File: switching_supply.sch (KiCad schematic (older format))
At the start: 0 parts

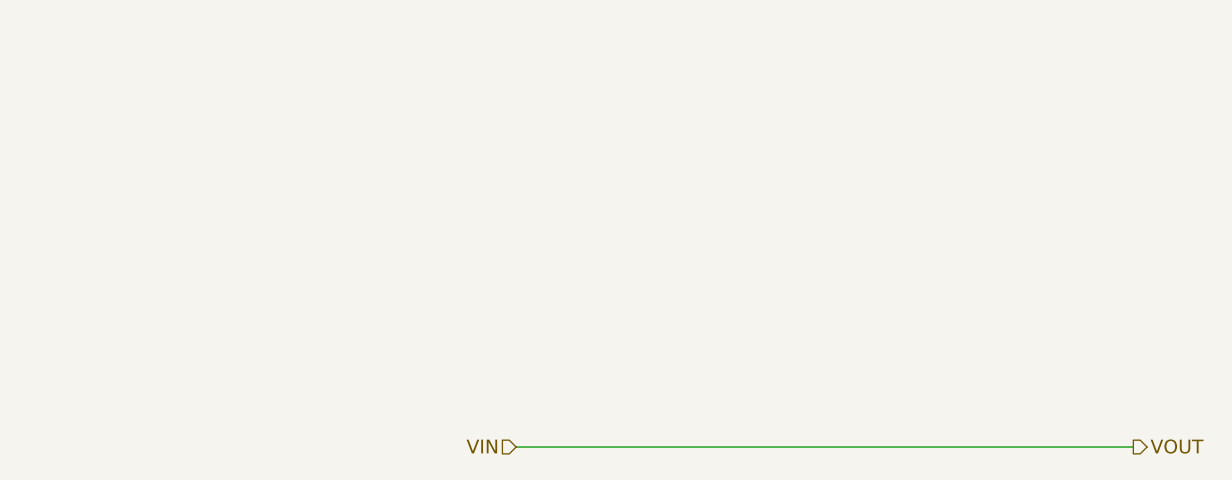
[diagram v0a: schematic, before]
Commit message: Esquematico completo. Footprintss asignados
Signed-off-by: Marcos Chaparro <mchaparro@paltatech.com>
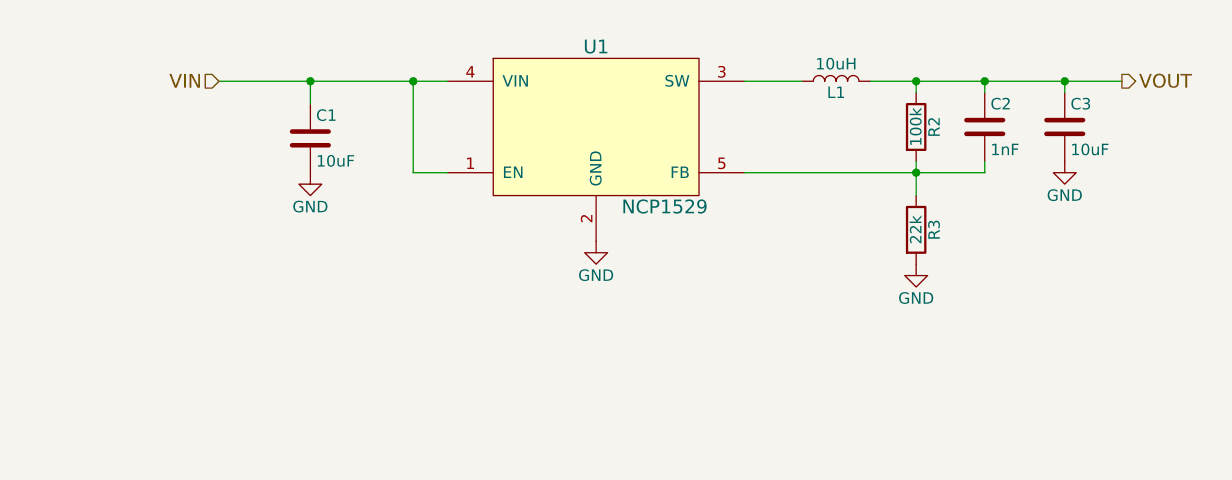
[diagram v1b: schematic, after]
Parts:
- added C1, C3: 10uF, Capacitors_SMD:C_0805, symbol C
- added C2: 1nF, Capacitors_SMD:C_0603, symbol C
- added L1: 10uH, Inductors_SMD:L_1812, symbol L
- added R2: 100k, Resistors_SMD:R_0603, symbol R
- added R3: 22k, Resistors_SMD:R_0603, symbol R
- added U1: NCP1529, TO_SOT_Packages_SMD:SOT-23-5, symbol NCP1529
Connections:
- net VIN: now also C1.1, U1.1 (EN), U1.4 (VIN)
- new net: L1.1, U1.3 (SW)
- new net: C2.2, R2.2, R3.1, U1.5 (FB)
- new net GND: C1.2, C3.2, R3.2, U1.2 (GND)
- new net VOUT: C2.1, C3.1, L1.2, R2.1
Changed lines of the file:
@@
 LIBS:contrib
 LIBS:valves
+LIBS:curso
+LIBS:bichito_e_luz-cache
 EELAYER 25 0
 EELAYER END
@@
 Comment4 ""
 $EndDescr
-Text HLabel 4900 4650 0    60   Input ~ 0
+Text HLabel 3600 3050 0    60   Input ~ 0
 VIN
-Text HLabel 7600 4650 2    60   Output ~ 0
+Text HLabel 7550 3050 2    60   Output ~ 0
 VOUT
+$Comp
+L NCP1529 U1
+U 1 1 59B19714
+P 5250 3350
+F 0 "U1" H 5250 3800 60  0000 C CNN
+F 1 "NCP1529" H 5550 3100 60  0000 C CNN
+F 2 "TO_SOT_Packages_SMD:SOT-23-5" H 5250 3350 60  0001 C CNN
+F 3 "" H 5250 3350 60  0001 C CNN
+	1    5250 3350
+	1    0    0    -1
+$EndComp
+$Comp
+L C C1
+U 1 1 59B1980A
+P 4000 3300
+F 0 "C1" H 4025 3400 50  0000 L CNN
+F 1 "10uF" H 4025 3200 50  0000 L CNN
+F 2 "Capacitors_SMD:C_0805" H 4038 3150 50  0001 C CNN
+F 3 "" H 4000 3300 50  0001 C CNN
+	1    4000 3300
+	1    0    0    -1
+$EndComp
+$Comp
+L L L1
+U 1 1 59B1986B
+P 6300 3050
+F 0 "L1" V 6250 3050 50  0000 C CNN
+F 1 "10uH" V 6375 3050 50  0000 C CNN
+F 2 "Inductors_SMD:L_1812" H 6300 3050 50  0001 C CNN
+F 3 "" H 6300 3050 50  0001 C CNN
+	1    6300 3050
+	0    -1   -1   0
+$EndComp
+$Comp
+L R R2
+U 1 1 59B198DA
+P 6650 3250
+F 0 "R2" V 6730 3250 50  0000 C CNN
+F 1 "100k" V 6650 3250 50  0000 C CNN
+F 2 "Resistors_SMD:R_0603" V 6580 3250 50  0001 C CNN
+F 3 "" H 6650 3250 50  0001 C CNN
+	1    6650 3250
+	1    0    0    -1
+$EndComp
+$Comp
+L R R3
+U 1 1 59B1995B
+P 6650 3700
+F 0 "R3" V 6730 3700 50  0000 C CNN
+F 1 "22k" V 6650 3700 50  0000 C CNN
+F 2 "Resistors_SMD:R_0603" V 6580 3700 50  0001 C CNN
+F 3 "" H 6650 3700 50  0001 C CNN
+	1    6650 3700
+	1    0    0    -1
+$EndComp
+$Comp
+L C C2
+U 1 1 59B1998D
+P 6950 3250
+F 0 "C2" H 6975 3350 50  0000 L CNN
+F 1 "1nF" H 6975 3150 50  0000 L CNN
+F 2 "Capacitors_SMD:C_0603" H 6988 3100 50  0001 C CNN
+F 3 "" H 6950 3250 50  0001 C CNN
+	1    6950 3250
+	1    0    0    -1
+$EndComp
+$Comp
+L C C3
+U 1 1 59B199F3
+P 7300 3250
+F 0 "C3" H 7325 3350 50  0000 L CNN
+F 1 "10uF" H 7325 3150 50  0000 L CNN
+F 2 "Capacitors_SMD:C_0805" H 7338 3100 50  0001 C CNN
+F 3 "" H 7300 3250 50  0001 C CNN
+	1    7300 3250
+	1    0    0    -1
+$EndComp
+$Comp
+L GND #PWR03
+U 1 1 59B19A47
+P 5250 3750
+F 0 "#PWR03" H 5250 3500 50  0001 C CNN
+F 1 "GND" H 5250 3600 50  0000 C CNN
+F 2 "" H 5250 3750 50  0001 C CNN
+F 3 "" H 5250 3750 50  0001 C CNN
+	1    5250 3750
+	1    0    0    -1
+$EndComp
 Wire Wire Line
-	4900 4650 7600 4650
+	3600 3050 4600 3050
+Wire Wire Line
+	4000 3150 4000 3050
+Connection ~ 4000 3050
+$Comp
+L GND #PWR04
+U 1 1 59B19AE4
+P 4000 3450
+F 0 "#PWR04" H 4000 3200 50  0001 C CNN
+F 1 "GND" H 4000 3300 50  0000 C CNN
+F 2 "" H 4000 3450 50  0001 C CNN
+F 3 "" H 4000 3450 50  0001 C CNN
+	1    4000 3450
+	1    0    0    -1
+$EndComp
+Wire Wire Line
+	4600 3450 4450 3450
+Wire Wire Line
+	4450 3450 4450 3050
+Connection ~ 4450 3050
+Wire Wire Line
+	5900 3050 6150 3050
+Wire Wire Line
+	6450 3050 7550 3050
+Wire Wire Line
+	6650 3050 6650 3100
+Wire Wire Line
+	6650 3400 6650 3550
+Wire Wire Line
+	5900 3450 6950 3450
+Connection ~ 6650 3450
+Wire Wire Line
+	6950 3050 6950 3100
+Connection ~ 6650 3050
+Wire Wire Line
+	6950 3450 6950 3400
+Wire Wire Line
+	7300 3050 7300 3100
+Connection ~ 6950 3050
+$Comp
+L GND #PWR05
+U 1 1 59B19BA3
+P 6650 3850
+F 0 "#PWR05" H 6650 3600 50  0001 C CNN
+F 1 "GND" H 6650 3700 50  0000 C CNN
+F 2 "" H 6650 3850 50  0001 C CNN
+F 3 "" H 6650 3850 50  0001 C CNN
+	1    6650 3850
+	1    0    0    -1
+$EndComp
+$Comp
+L GND #PWR06
+U 1 1 59B19BC3
+P 7300 3400
+F 0 "#PWR06" H 7300 3150 50  0001 C CNN
+F 1 "GND" H 7300 3250 50  0000 C CNN
+F 2 "" H 7300 3400 50  0001 C CNN
+F 3 "" H 7300 3400 50  0001 C CNN
+	1    7300 3400
+	1    0    0    -1
+$EndComp
+Connection ~ 7300 3050
 $EndSCHEMATC

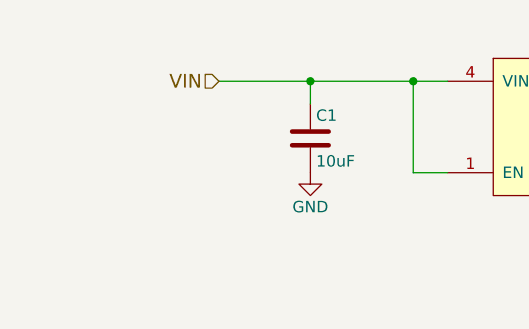
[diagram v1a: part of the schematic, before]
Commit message: Termino layout. Despues de la clase agregue silkscreens y un fusible
Signed-off-by: Marcos Chaparro <mchaparro@paltatech.com>
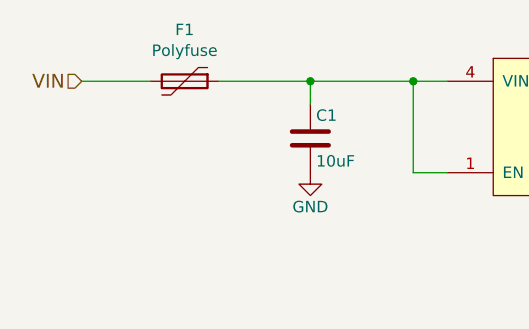
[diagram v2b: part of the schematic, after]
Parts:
- added F1: Polyfuse, Resistors_SMD:R_0805, symbol Polyfuse
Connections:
- net VIN: now also F1.2; no longer C1.1, U1.1 (EN), U1.4 (VIN)
- new net: C1.1, F1.1, U1.1 (EN), U1.4 (VIN)
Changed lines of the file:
@@
 Comment4 ""
 $EndDescr
-Text HLabel 3600 3050 0    60   Input ~ 0
+Text HLabel 3000 3050 0    60   Input ~ 0
 VIN
 Text HLabel 7550 3050 2    60   Output ~ 0
@@
 $EndComp
 Connection ~ 7300 3050
+$Comp
+L Polyfuse F1
+U 1 1 59BA7D61
+P 3450 3050
+F 0 "F1" V 3225 3050 50  0000 C CNN
+F 1 "Polyfuse" V 3316 3050 50  0000 C CNN
+F 2 "Resistors_SMD:R_0805" H 3500 2850 50  0001 L CNN
+F 3 "" H 3450 3050 50  0001 C CNN
+F 4 "0" H 3450 3050 60  0001 C CNN "Exclude from BOM"
+	1    3450 3050
+	0    1    1    0
+$EndComp
+Wire Wire Line
+	3300 3050 3000 3050
 $EndSCHEMATC

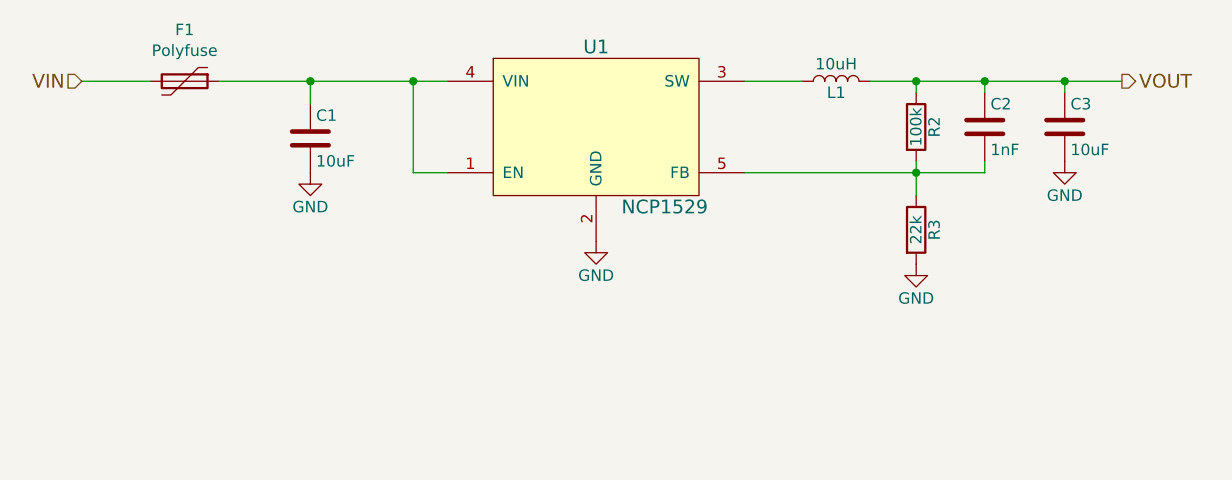
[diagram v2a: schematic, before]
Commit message: Add pulldowns updated values and assembly layer
Signed-off-by: Marcos Chaparro <mchaparro@paltatech.com>
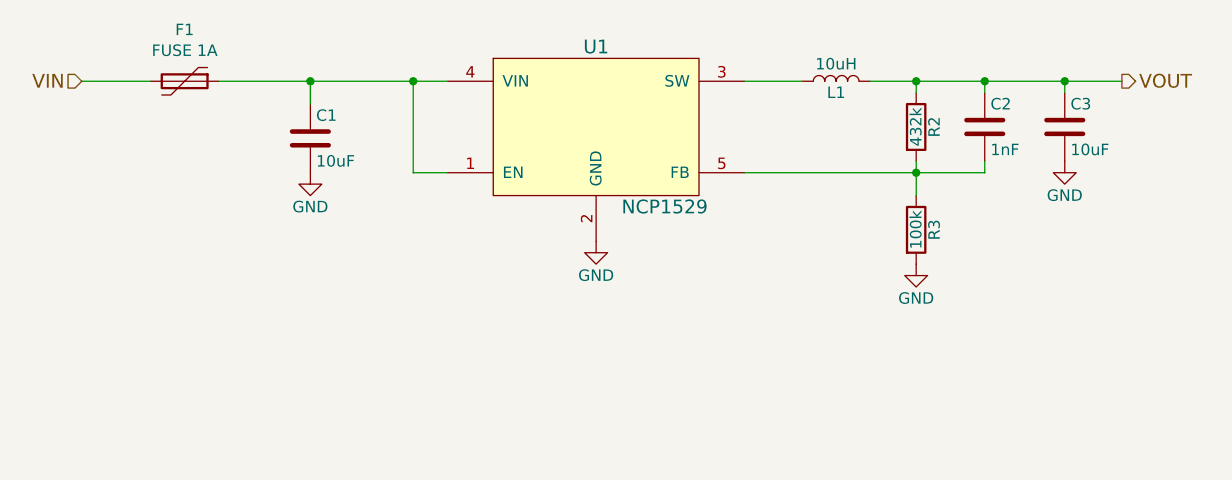
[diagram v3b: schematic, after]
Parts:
- F1: value Polyfuse -> FUSE 1A; MPN (none) -> 0ZCK0050FF2E
- L1: MPN (none) -> LQH43PN100M26L
- R2: value 100k -> 432k
- R3: value 22k -> 100k
- U1: MPN (none) -> NCP1529ASNT1G
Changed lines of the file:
@@
-EESchema Schematic File Version 2
+EESchema Schematic File Version 3
 LIBS:power
 LIBS:device
@@
 LIBS:contrib
 LIBS:valves
-LIBS:curso
 LIBS:bichito_e_luz-cache
-EELAYER 25 0
+EELAYER 26 0
 EELAYER END
 $Descr A4 11693 8268
@@
 F 2 "TO_SOT_Packages_SMD:SOT-23-5" H 5250 3350 60  0001 C CNN
 F 3 "" H 5250 3350 60  0001 C CNN
+F 4 "NCP1529ASNT1G" H 0   0   60  0001 C CNN "MPN"
 	1    5250 3350
 	1    0    0    -1
@@
 F 2 "Inductors_SMD:L_1812" H 6300 3050 50  0001 C CNN
 F 3 "" H 6300 3050 50  0001 C CNN
+F 4 "LQH43PN100M26L" H 0   0   60  0001 C CNN "MPN"
 	1    6300 3050
 	0    -1   -1   0
@@
 P 6650 3250
 F 0 "R2" V 6730 3250 50  0000 C CNN
-F 1 "100k" V 6650 3250 50  0000 C CNN
+F 1 "432k" V 6650 3250 50  0000 C CNN
 F 2 "Resistors_SMD:R_0603" V 6580 3250 50  0001 C CNN
 F 3 "" H 6650 3250 50  0001 C CNN
@@
 P 6650 3700
 F 0 "R3" V 6730 3700 50  0000 C CNN
-F 1 "22k" V 6650 3700 50  0000 C CNN
+F 1 "100k" V 6650 3700 50  0000 C CNN
 F 2 "Resistors_SMD:R_0603" V 6580 3700 50  0001 C CNN
 F 3 "" H 6650 3700 50  0001 C CNN
@@
 P 3450 3050
 F 0 "F1" V 3225 3050 50  0000 C CNN
-F 1 "Polyfuse" V 3316 3050 50  0000 C CNN
+F 1 "FUSE 1A" V 3316 3050 50  0000 C CNN
 F 2 "Resistors_SMD:R_0805" H 3500 2850 50  0001 L CNN
 F 3 "" H 3450 3050 50  0001 C CNN
 F 4 "0" H 3450 3050 60  0001 C CNN "Exclude from BOM"
+F 5 "0ZCK0050FF2E" H 0   0   60  0001 C CNN "MPN"
 	1    3450 3050
 	0    1    1    0
